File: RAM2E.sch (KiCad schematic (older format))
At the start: 63 parts, among them J1 AppleIIeAux, J2 JTAG, U1 EPM240T100, U2 W9864G6KH-6, U3 74AHC245, U4 74LVC245, U5 74AHC245, U6 74AHCT245, U7 74AHCT245, U8 TPS73701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

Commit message: As submitted to JLCPCB August 2020
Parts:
- removed C30: DNP, stdpads:C_0805, symbol Device:C_Small
- removed R1: 5k76, stdpads:R_0805, symbol Device:R_Small
- removed R2: 3k3, stdpads:R_0805, symbol Device:R_Small
- removed R3, R4, R8: DNP, stdpads:R_0805, symbol Device:R_Small
- removed R5: 0, stdpads:R_0805, symbol Device:R_Small
- removed U8: TPS73701, stdpads:SOT-223-6, symbol GW_Power:TPS73701
- removed U9: DNP, stdpads:SOT-223-6, symbol GW_Power:TPS73701
- added U8: AP2125N-3.3, stdpads:SOT-23, symbol GW_Power:AP2125
- C1, C2, C29, C3, C4, C5, C6: LCSC Part (none) -> C15850
- C10, C11, C12, C13, C14, C15, C16, C17, C18, C19, C20, C21, C22, C23, C24, C25, C26, C27, C28, C7, C8, C9: LCSC Part (none) -> C23630
- H1, H2, H3, H4: footprint stdpads:PasteHole_1.1mm_PTH -> stdpads:PasteHole_1.152mm_NPTH
- R10: LCSC Part (none) -> C17560
- R6: LCSC Part (none) -> C17477
- R9: value 1k2 -> 22k; LCSC Part (none) -> C17560
- RN1, RN2, RN3: value 4x100 -> 4x33; footprint stdpads:Yageo_YC124 -> stdpads:R4_0402; LCSC Part (none) -> C25501
- U1: LCSC Part (none) -> C10041
- U2: value W9864G6KH-6 -> W9812G6KH-6; LCSC Part (none) -> C62379
- U3, U5: LCSC Part (none) -> C5516
- U4: LCSC Part (none) -> C6082
- U6, U7: LCSC Part (none) -> C173388
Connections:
- net +1V8 is gone; now on net +3V3: C16.1, C19.1, C5.1, C6.1, U1.13 (VCCINT), U1.63 (VCCINT)
- net +3V3: now also C2.1, U8.2 (Vout)
- net +5V: now also U8.3 (Vin); no longer C2.1
- net ACLK: no longer RN3.6 (R3.2)
- net GND: now also U2.36 (A12), U8.1 (GND)
- net RCLK: no longer RN3.7 (R2.2)
- net at RN3.1 (R1.1), RN3.4 (R4.1), U4.18 (B0): no longer RN3.2 (R2.1), RN3.3 (R3.1)
- net CFG0: no longer names the net of U1.87 (IO2_87)
- net CFG1: no longer names the net of U1.86 (IO2_86)
- net CFG2: no longer names the net of U1.88 (IO2_88)
- net DlyIn: no longer names the net of U1.82 (IO2_82)
- net DlyOut: no longer names the net of U1.83 (IO2_83)
- no-connect marks 8 -> 17
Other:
- moved on the sheet: C1, C10, C11, C12, C13, C14, C15, C16, C17, C18, C19, C20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

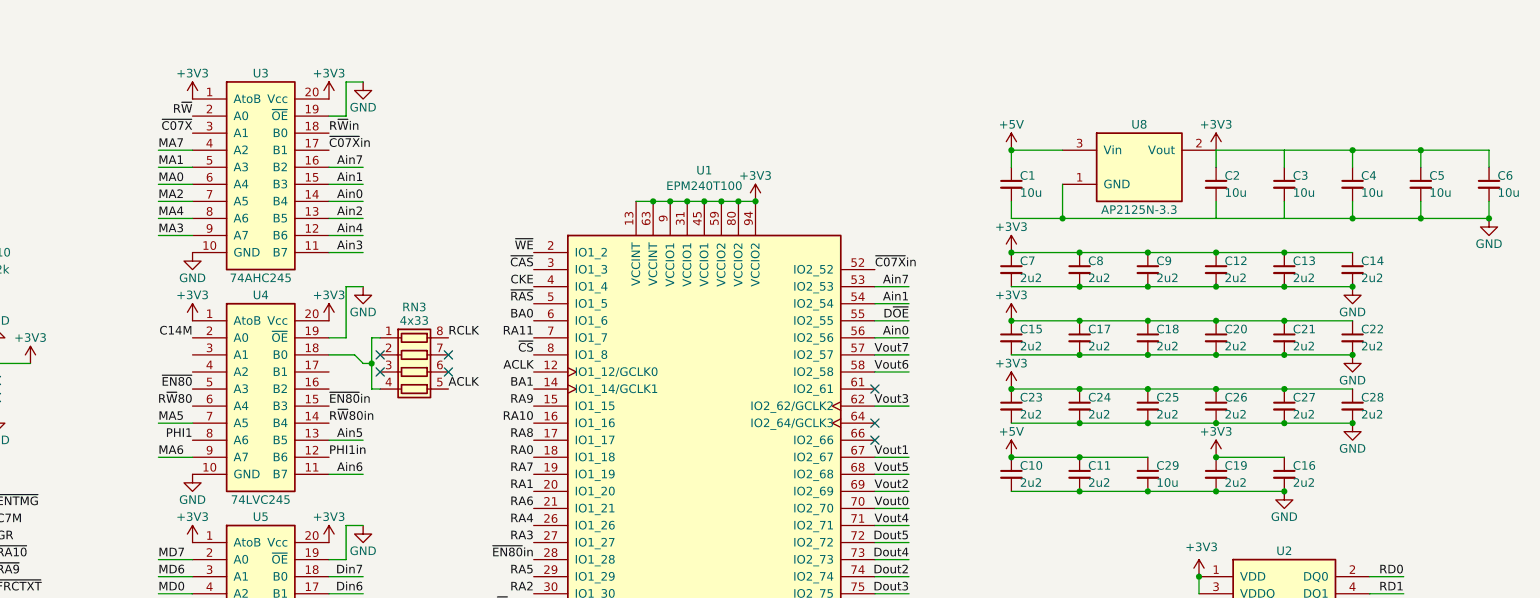
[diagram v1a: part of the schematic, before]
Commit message: Updated schematic with 1V8 regulator and MAX V
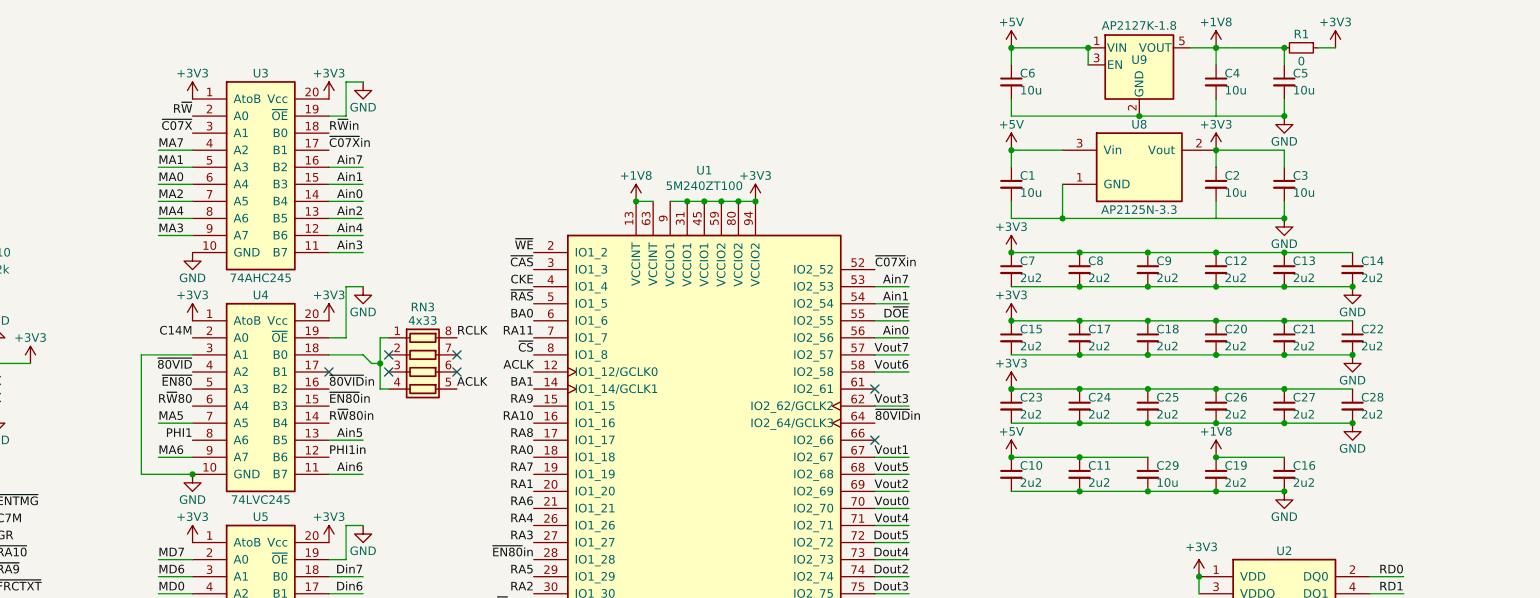
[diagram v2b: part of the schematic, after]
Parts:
- added R1: 0, stdpads:R_0805, symbol Device:R_Small
- added U9: AP2127K-1.8, stdpads:SOT-23-5, symbol Regulator_Linear:AP2127K-1.8
- U1: value EPM240T100 -> 5M240ZT100
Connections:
- net +3V3: now also R1.1; no longer C16.1, C19.1, C4.1, C5.1, C6.1, U1.13 (VCCINT), U1.63 (VCCINT)
- net +5V: now also C6.1, U9.1 (VIN), U9.3 (EN)
- net GND: now also U4.3 (A1), U9.2 (GND)
- net ~80VID~: now also U4.4 (A2)
- net ~80VID~in: now reaches U1.64 (IO2_64/GCLK3)
- net ~80VID~in: now also U4.16 (B2)
- new net +1V8: C16.1, C19.1, C4.1, C5.1, R1.2, U1.13 (VCCINT), U1.63 (VCCINT), U9.5 (VOUT)
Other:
- moved on the sheet: C4, C5, RN3

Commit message: Merge branch 'dev-GW4203B-1.2' of https://github.com/garrettsworkshop/RAM2E into dev-GW4203B-1.2
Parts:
- added RN4, RN5: 4x33, stdpads:R4_0402, symbol Device:R_Pack04
- R1: value 0 -> DNP
- U1: LCSC Part C10041 -> C192889
- U3, U5: value 74AHC245 -> 74LVC245; LCSC Part C5516 -> C6082
- U8: value AP2125N-3.3 -> XC6206P332MR; LCSC Part C150715 -> C5446
- U9: LCSC Part (none) -> C151375
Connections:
- net Ain0: now also RN5.8 (R1.2); no longer U3.14 (B4)
- net Ain1: now also RN4.5 (R4.2); no longer U3.15 (B3)
- net Ain2: now also RN5.7 (R2.2); no longer U3.13 (B5)
- net Ain3: now also RN5.5 (R4.2); no longer U3.11 (B7)
- net Ain4: now also RN5.6 (R3.2); no longer U3.12 (B6)
- net Ain7: now also RN4.6 (R3.2); no longer U3.16 (B2)
- net GND: now also U4.4 (A2)
- net R~W~in: now also RN4.8 (R1.2); no longer U3.18 (B0)
- net ~80VID~: no longer U4.4 (A2)
- net ~80VID~in: no longer U4.16 (B2)
- net ~C07X~in: now also RN4.7 (R2.2); no longer U3.17 (B1)
- new net: RN5.4 (R4.1), U3.11 (B7)
- new net: RN5.3 (R3.1), U3.12 (B6)
- new net: RN5.2 (R2.1), U3.13 (B5)
- new net: RN5.1 (R1.1), U3.14 (B4)
- new net: RN4.4 (R4.1), U3.15 (B3)
- new net: RN4.3 (R3.1), U3.16 (B2)
- new net: RN4.2 (R2.1), U3.17 (B1)
- new net: RN4.1 (R1.1), U3.18 (B0)
- no-connect marks 17 -> 18
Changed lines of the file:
@@
 Sheet 1 2
 Title "GW4203B (RAM2E II)"
-Date "2020-08-04"
-Rev "1.1"
+Date "2020-09-10"
+Rev "1.2"
 Comp "Garrett's Workshop"
 Comment1 ""
@@
 P 3000 1500
 F 0 "U3" H 3000 2100 50  0000 C CNN
-F 1 "74AHC245" H 3000 900 50  0000 C CNN
+F 1 "74LVC245" H 3000 900 50  0000 C CNN
 F 2 "stdpads:TSSOP-20_4.4x6.5mm_P0.65mm" H 3000 850 50  0001 C TNN
 F 3 "" H 3000 1600 60  0001 C CNN
-F 4 "C5516" H 3000 1500 50  0001 C CNN "LCSC Part"
+F 4 "C6082" H 3000 1500 50  0001 C CNN "LCSC Part"
 	1    3000 1500
 	1    0    0    -1
@@
 L power:GND #PWR0104
 U 1 1 5E9BEAE2
-P 3600 950
-F 0 "#PWR0104" H 3600 700 50  0001 C CNN
-F 1 "GND" H 3600 800 50  0000 C CNN
-F 2 "" H 3600 950 50  0001 C CNN
-F 3 "" H 3600 950 50  0001 C CNN
-	1    3600 950
-	1    0    0    -1
-$EndComp
-Wire Wire Line
-	3500 1150 3500 950
-Wire Wire Line
-	3500 950  3600 950
+P 3600 850
+F 0 "#PWR0104" H 3600 600 50  0001 C CNN
+F 1 "GND" H 3600 700 50  0000 C CNN
+F 2 "" H 3600 850 50  0001 C CNN
+F 3 "" H 3600 850 50  0001 C CNN
+	1    3600 850
+	1    0    0    -1
+$EndComp
+Wire Wire Line
+	3500 850  3600 850
 Wire Wire Line
 	3400 1150 3500 1150
@@
 Wire Wire Line
 	8500 5150 8300 5150
-Text Label 3400 1350 0    50   ~ 0
+Text Label 3800 1350 0    50   ~ 0
 ~C07X~in
 Text Label 3400 2950 0    50   ~ 0
@@
 Text Label 3400 2850 0    50   ~ 0
 ~EN80~in
-Text Label 3400 1250 0    50   ~ 0
+Text Label 3800 1250 0    50   ~ 0
 R~W~in
 Text Label 3400 3150 0    50   ~ 0
@@
 P 3000 4100
 F 0 "U5" H 3000 4700 50  0000 C CNN
-F 1 "74AHC245" H 3000 3500 50  0000 C CNN
+F 1 "74LVC245" H 3000 3500 50  0000 C CNN
 F 2 "stdpads:TSSOP-20_4.4x6.5mm_P0.65mm" H 3000 3450 50  0001 C TNN
 F 3 "" H 3000 4200 60  0001 C CNN
-F 4 "C5516" H 3000 4100 50  0001 C CNN "LCSC Part"
+F 4 "C6082" H 3000 4100 50  0001 C CNN "LCSC Part"
 	1    3000 4100
 	1    0    0    -1
@@
 L power:GND #PWR0126
 U 1 1 5F3A4A01
-P 3600 2150
-F 0 "#PWR0126" H 3600 1900 50  0001 C CNN
-F 1 "GND" H 3600 2000 50  0000 C CNN
-F 2 "" H 3600 2150 50  0001 C CNN
-F 3 "" H 3600 2150 50  0001 C CNN
-	1    3600 2150
-	1    0    0    -1
-$EndComp
-Wire Wire Line
-	3500 2150 3600 2150
+P 3600 2350
+F 0 "#PWR0126" H 3600 2100 50  0001 C CNN
+F 1 "GND" H 3600 2200 50  0000 C CNN
+F 2 "" H 3600 2350 50  0001 C CNN
+F 3 "" H 3600 2350 50  0001 C CNN
+	1    3600 2350
+	1    0    0    -1
+$EndComp
+Wire Wire Line
+	3500 2350 3600 2350
 Wire Wire Line
 	3400 2450 3500 2450
@@
 R~W~80
 Wire Wire Line
-	3600 1750 3400 1750
-Wire Wire Line
-	3600 1950 3400 1950
-Wire Wire Line
-	3600 1850 3400 1850
+	4000 1750 3800 1750
+Wire Wire Line
+	4000 1950 3800 1950
+Wire Wire Line
+	4000 1850 3800 1850
 Wire Wire Line
 	3600 3050 3400 3050
 Wire Wire Line
-	3600 1450 3400 1450
-Text Label 3600 1750 2    50   ~ 0
+	4000 1450 3800 1450
+Text Label 4000 1750 2    50   ~ 0
 Ain2
-Text Label 3600 1950 2    50   ~ 0
+Text Label 4000 1950 2    50   ~ 0
 Ain3
 Text Label 3600 3250 2    50   ~ 0
 Ain6
-Text Label 3600 1850 2    50   ~ 0
+Text Label 4000 1850 2    50   ~ 0
 Ain4
 Text Label 3600 3050 2    50   ~ 0
 Ain5
-Text Label 3600 1450 2    50   ~ 0
+Text Label 4000 1450 2    50   ~ 0
 Ain7
 Wire Wire Line
-	3600 1550 3400 1550
-Text Label 3600 1650 2    50   ~ 0
+	4000 1550 3800 1550
+Text Label 4000 1650 2    50   ~ 0
 Ain0
-Text Label 3600 1550 2    50   ~ 0
+Text Label 4000 1550 2    50   ~ 0
 Ain1
 Wire Wire Line
-	3600 1650 3400 1650
+	4000 1650 3800 1650
 Text Label 2600 1150 2    50   ~ 0
 R~W~
@@
 Wire Wire Line
 	5200 1650 5300 1650
-Wire Wire Line
-	3500 2150 3500 2450
 Text Label 4150 2750 0    50   ~ 0
 ACLK
@@
 F 2 "stdpads:TQFP-100_14x14mm_P0.5mm" H 6000 1700 50  0001 L CNN
 F 3 "https://www.altera.com/content/dam/altera-www/global/en_US/pdfs/literature/hb/max2/max2_mii5v1.pdf" H 5600 4050 50  0001 C CNN
-F 4 "C10041" H 5600 4050 50  0001 C CNN "LCSC Part"
+F 4 "C192889" H 5600 4050 50  0001 C CNN "LCSC Part"
 	1    5600 4050
 	1    0    0    -1
@@
 P 8150 1450
 F 0 "U8" H 8150 1700 50  0000 C CNN
-F 1 "AP2125N-3.3" H 8150 1200 50  0000 C CNN
+F 1 "XC6206P332MR" H 8150 1200 50  0000 C CNN
 F 2 "stdpads:SOT-23" H 8150 1150 50  0001 C TNN
 F 3 "" H 8150 1350 60  0001 C CNN
-F 4 "C150715" H 8150 1450 50  0001 C CNN "LCSC Part"
+F 4 "C5446" H 8150 1450 50  0001 C CNN "LCSC Part"
 	1    8150 1450
 	1    0    0    -1
@@
 Wire Wire Line
 	8600 1750 8600 1650
-Text Label 2600 2650 2    50   ~ 0
-~80VID~
-Text Label 3400 2750 0    50   ~ 0
-~80VID~in
 Wire Wire Line
 	3600 2550 3650 2600
@@
 	3400 2550 3600 2550
 NoConn ~ 3400 2650
-Wire Wire Line
-	2600 2550 2300 2550
 Wire Wire Line
 	2300 2550 2300 3250
@@
 F 2 "stdpads:SOT-23-5" H 8150 1175 50  0001 C CNN
 F 3 "https://www.diodes.com/assets/Datasheets/AP2127.pdf" H 8150 950 50  0001 C CNN
+F 4 "C151375" H 8150 850 50  0001 C CNN "LCSC Part"
 	1    8150 850
 	1    0    0    -1
@@
 P 9100 750
 F 0 "R1" V 9050 750 50  0000 C BNN
-F 1 "0" V 9150 750 50  0000 C TNN
+F 1 "DNP" V 9150 750 50  0000 C TNN
 F 2 "stdpads:R_0805" H 9100 750 50  0001 C CNN
 F 3 "~" H 9100 750 50  0001 C CNN
@@
 Wire Wire Line
 	9300 750  9200 750
+Wire Wire Line
+	2600 2550 2300 2550
+Wire Wire Line
+	2600 2550 2600 2650
+Connection ~ 2600 2550
+NoConn ~ 3400 2750
+$Comp
+L Device:R_Pack04 RN5
+U 1 1 5F6F2814
+P 3600 1850
+F 0 "RN5" V 3900 1850 50  0000 C BNN
+F 1 "4x33" V 3800 1850 50  0000 C CNN
+F 2 "stdpads:R4_0402" V 3875 1850 50  0001 C CNN
+F 3 "~" H 3600 1850 50  0001 C CNN
+F 4 "C25501" H 3600 1850 50  0001 C CNN "LCSC Part"
+	1    3600 1850
+	0    1    1    0
+$EndComp
+$Comp
+L Device:R_Pack04 RN4
+U 1 1 5F68B09A
+P 3600 1450
+F 0 "RN4" V 3250 1450 50  0000 C BNN
+F 1 "4x33" V 3300 1450 50  0000 C CNN
+F 2 "stdpads:R4_0402" V 3875 1450 50  0001 C CNN
+F 3 "~" H 3600 1450 50  0001 C CNN
+F 4 "C25501" H 3600 1450 50  0001 C CNN "LCSC Part"
+	1    3600 1450
+	0    1    1    0
+$EndComp
+Wire Wire Line
+	3500 850  3500 1150
+Wire Wire Line
+	3500 2350 3500 2450
 Wire Bus Line
 	8200 4250 8200 5350

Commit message: Actually fabbed 10/6/2020
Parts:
- U1: value 5M240ZT100 -> 5M240ZT100C5N
- U3, U4, U5: value 74LVC245 -> 74LVC245APW
- U6, U7: value 74AHCT245 -> 74AHCT245PW
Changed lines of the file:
@@
 Sheet 1 2
 Title "GW4203B (RAM2E II)"
-Date "2020-09-10"
+Date "2020-09-29"
 Rev "1.2"
 Comp "Garrett's Workshop"
@@
 P 3000 1500
 F 0 "U3" H 3000 2100 50  0000 C CNN
-F 1 "74LVC245" H 3000 900 50  0000 C CNN
+F 1 "74LVC245APW" H 3000 900 50  0000 C CNN
 F 2 "stdpads:TSSOP-20_4.4x6.5mm_P0.65mm" H 3000 850 50  0001 C TNN
 F 3 "" H 3000 1600 60  0001 C CNN
@@
 P 3000 5400
 F 0 "U6" H 3000 6000 50  0000 C CNN
-F 1 "74AHCT245" H 3000 4800 50  0000 C CNN
+F 1 "74AHCT245PW" H 3000 4800 50  0000 C CNN
 F 2 "stdpads:TSSOP-20_4.4x6.5mm_P0.65mm" H 3000 4750 50  0001 C TNN
 F 3 "" H 3000 5500 60  0001 C CNN
@@
 P 3000 4100
 F 0 "U5" H 3000 4700 50  0000 C CNN
-F 1 "74LVC245" H 3000 3500 50  0000 C CNN
+F 1 "74LVC245APW" H 3000 3500 50  0000 C CNN
 F 2 "stdpads:TSSOP-20_4.4x6.5mm_P0.65mm" H 3000 3450 50  0001 C TNN
 F 3 "" H 3000 4200 60  0001 C CNN
@@
 P 3000 6700
 F 0 "U7" H 3000 7300 50  0000 C CNN
-F 1 "74AHCT245" H 3000 6100 50  0000 C CNN
+F 1 "74AHCT245PW" H 3000 6100 50  0000 C CNN
 F 2 "stdpads:TSSOP-20_4.4x6.5mm_P0.65mm" H 3000 6050 50  0001 C TNN
 F 3 "" H 3000 6800 60  0001 C CNN
@@
 P 3000 2800
 F 0 "U4" H 3000 3400 50  0000 C CNN
-F 1 "74LVC245" H 3000 2200 50  0000 C CNN
+F 1 "74LVC245APW" H 3000 2200 50  0000 C CNN
 F 2 "stdpads:TSSOP-20_4.4x6.5mm_P0.65mm" H 3000 2150 50  0001 C TNN
 F 3 "" H 3000 2900 60  0001 C CNN
@@
 U 1 1 5EF407E5
 P 5600 4050
-F 0 "U1" H 5600 6631 50  0000 C CNN
-F 1 "5M240ZT100" H 5600 6540 50  0000 C CNN
+F 0 "U1" H 5550 6550 50  0000 C BNN
+F 1 "5M240ZT100C5N" H 5550 6500 50  0000 C CNN
 F 2 "stdpads:TQFP-100_14x14mm_P0.5mm" H 6000 1700 50  0001 L CNN
 F 3 "https://www.altera.com/content/dam/altera-www/global/en_US/pdfs/literature/hb/max2/max2_mii5v1.pdf" H 5600 4050 50  0001 C CNN

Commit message: Added C14M buffering and header
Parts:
- added J3: C14M, Connector_PinHeader_2.54mm:PinHeader_1x02_P2.54mm_Vertical, symbol Connector_Generic:Conn_01x02
- added R2, R3: 33, stdpads:R_0603, symbol Device:R_Small
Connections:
- net C14M: now also R2.2; no longer U4.2 (A0)
- net GND: now also J3.2 (Pin_2); no longer U4.4 (A2)
- net at U4.16 (B2): now also R3.2
- new net C14MB: J3.1 (Pin_1), R3.1
- new net C14MR: R2.1, U4.2 (A0), U4.4 (A2)
- no-connect marks 18 -> 17
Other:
- moved on the sheet: RN3
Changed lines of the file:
@@
 Text Label 2400 1450 0    50   ~ 0
 MA1
-Text Label 2600 2450 2    50   ~ 0
+Text Label 2150 2450 2    50   ~ 0
 C14M
 $Comp
@@
 Text Label 4600 2650 2    50   ~ 0
 ACLK
-Text Label 4150 2450 0    50   ~ 0
+Text Label 4150 2300 0    50   ~ 0
 RCLK
 Text Label 4600 2850 2    50   ~ 0
@@
 Wire Wire Line
 	5200 1650 5300 1650
-Text Label 4150 2750 0    50   ~ 0
+Text Label 4150 2600 0    50   ~ 0
 ACLK
 $Comp
 L Device:R_Pack04 RN3
 U 1 1 5F475CD8
-P 3950 2650
-F 0 "RN3" V 3600 2650 50  0000 C BNN
-F 1 "4x33" V 3650 2650 50  0000 C CNN
-F 2 "stdpads:R4_0402" V 4225 2650 50  0001 C CNN
-F 3 "~" H 3950 2650 50  0001 C CNN
-F 4 "C25501" H 3950 2650 50  0001 C CNN "LCSC Part"
-	1    3950 2650
+P 3950 2500
+F 0 "RN3" V 3600 2500 50  0000 C BNN
+F 1 "4x33" V 3650 2500 50  0000 C CNN
+F 2 "stdpads:R4_0402" V 4225 2500 50  0001 C CNN
+F 3 "~" H 3950 2500 50  0001 C CNN
+F 4 "C25501" H 3950 2500 50  0001 C CNN "LCSC Part"
+	1    3950 2500
 	0    1    1    0
 $EndComp
@@
 NoConn ~ 6600 5050
 Wire Wire Line
-	3750 2450 3700 2450
-Wire Wire Line
-	3700 2750 3750 2750
-NoConn ~ 4150 2550
-NoConn ~ 4150 2650
-NoConn ~ 3750 2550
-NoConn ~ 3750 2650
-Wire Wire Line
-	3700 2450 3700 2600
+	3750 2300 3700 2300
+Wire Wire Line
+	3700 2600 3750 2600
+NoConn ~ 4150 2400
+NoConn ~ 4150 2500
+NoConn ~ 3750 2400
+NoConn ~ 3750 2500
 Wire Wire Line
 	3650 2600 3700 2600
 Connection ~ 3700 2600
-Wire Wire Line
-	3700 2600 3700 2750
 $Comp
 L power:GND #PWR0146
@@
 NoConn ~ 3400 2650
 Wire Wire Line
-	2300 2550 2300 3250
-Wire Wire Line
 	2300 3250 2600 3250
 Connection ~ 2600 3250
@@
 Wire Wire Line
 	9300 750  9200 750
-Wire Wire Line
-	2600 2550 2300 2550
-Wire Wire Line
-	2600 2550 2600 2650
-Connection ~ 2600 2550
-NoConn ~ 3400 2750
 $Comp
 L Device:R_Pack04 RN5
@@
 Wire Wire Line
 	3500 2350 3500 2450
+Wire Wire Line
+	2600 2550 2300 2550
+Wire Wire Line
+	2300 2550 2300 3250
+Wire Wire Line
+	2500 2450 2500 2650
+Wire Wire Line
+	2500 2650 2600 2650
+Wire Wire Line
+	2600 2450 2500 2450
+Wire Wire Line
+	3700 2300 3700 2600
+$Comp
+L Device:R_Small R3
+U 1 1 6081D682
+P 3950 2750
+F 0 "R3" V 4000 2750 50  0000 C TNN
+F 1 "33" V 4100 2750 50  0000 C CNN
+F 2 "stdpads:R_0603" H 3950 2750 50  0001 C CNN
+F 3 "~" H 3950 2750 50  0001 C CNN
+	1    3950 2750
+	0    1    1    0
+$EndComp
+Wire Wire Line
+	3400 2750 3850 2750
+$Comp
+L Connector_Generic:Conn_01x02 J3
+U 1 1 608879CA
+P 1050 1150
+F 0 "J3" H 1050 1250 50  0000 C CNN
+F 1 "C14M" H 1050 950 50  0000 C CNN
+F 2 "Connector_PinHeader_2.54mm:PinHeader_1x02_P2.54mm_Vertical" H 1050 1150 50  0001 C CNN
+F 3 "~" H 1050 1150 50  0001 C CNN
+	1    1050 1150
+	-1   0    0    -1
+$EndComp
+Text Label 1250 1150 0    50   ~ 0
+C14MB
+$Comp
+L power:GND #PWR0147
+U 1 1 6088870C
+P 1250 1250
+F 0 "#PWR0147" H 1250 1000 50  0001 C CNN
+F 1 "GND" H 1250 1100 50  0000 C CNN
+F 2 "" H 1250 1250 50  0001 C CNN
+F 3 "" H 1250 1250 50  0001 C CNN
+	1    1250 1250
+	1    0    0    -1
+$EndComp
+Text Label 4050 2750 0    50   ~ 0
+C14MB
+$Comp
+L Device:R_Small R2
+U 1 1 6088A353
+P 2250 2450
+F 0 "R2" V 2400 2450 50  0000 C CNN
+F 1 "33" V 2300 2450 50  0000 C TNN
+F 2 "stdpads:R_0603" H 2250 2450 50  0001 C CNN
+F 3 "~" H 2250 2450 50  0001 C CNN
+	1    2250 2450
+	0    1    -1   0
+$EndComp
+Text Label 2600 2450 2    50   ~ 0
+C14MR
+Wire Wire Line
+	2350 2450 2500 2450
 Wire Bus Line
 	8200 4250 8200 5350
+Connection ~ 2500 2450
 $EndSCHEMATC

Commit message: Fabbed
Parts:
- R1: value DNP -> 0; LCSC Part (none) -> C17477
- R2, R3: value 33 -> 47; LCSC Part (none) -> C23182
- U1: value 5M240ZT100C5N -> EPM240T100C5N; LCSC Part C192889 -> C10041
- U9: value AP2127K-1.8 -> DNP; LCSC Part C151375 -> (none)
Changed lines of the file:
@@
 Sheet 1 2
 Title "GW4203B (RAM2E II)"
-Date "2020-09-29"
-Rev "1.2"
+Date "2020-12-25"
+Rev "1.3"
 Comp "Garrett's Workshop"
 Comment1 ""
@@
 P 5600 4050
 F 0 "U1" H 5550 6550 50  0000 C BNN
-F 1 "5M240ZT100C5N" H 5550 6500 50  0000 C CNN
+F 1 "EPM240T100C5N" H 5550 6500 50  0000 C CNN
 F 2 "stdpads:TQFP-100_14x14mm_P0.5mm" H 6000 1700 50  0001 L CNN
 F 3 "https://www.altera.com/content/dam/altera-www/global/en_US/pdfs/literature/hb/max2/max2_mii5v1.pdf" H 5600 4050 50  0001 C CNN
-F 4 "C192889" H 5600 4050 50  0001 C CNN "LCSC Part"
+F 4 "C10041" H 5600 4050 50  0001 C CNN "LCSC Part"
 	1    5600 4050
 	1    0    0    -1
@@
 	3400 2550 3600 2550
 NoConn ~ 3400 2650
-Wire Wire Line
-	2300 3250 2600 3250
 Connection ~ 2600 3250
 Text Label 6600 2950 0    50   ~ 0
@@
 P 8150 850
 F 0 "U9" H 8150 850 50  0000 C BNN
-F 1 "AP2127K-1.8" H 8150 1050 50  0000 C BNN
+F 1 "DNP" H 8150 1050 50  0000 C BNN
 F 2 "stdpads:SOT-23-5" H 8150 1175 50  0001 C CNN
 F 3 "https://www.diodes.com/assets/Datasheets/AP2127.pdf" H 8150 950 50  0001 C CNN
-F 4 "C151375" H 8150 850 50  0001 C CNN "LCSC Part"
+F 4 "" H 8150 850 50  0001 C CNN "LCSC Part"
 	1    8150 850
 	1    0    0    -1
@@
 P 9100 750
 F 0 "R1" V 9050 750 50  0000 C BNN
-F 1 "DNP" V 9150 750 50  0000 C TNN
+F 1 "0" V 9150 750 50  0000 C TNN
 F 2 "stdpads:R_0805" H 9100 750 50  0001 C CNN
 F 3 "~" H 9100 750 50  0001 C CNN
+F 4 "C17477" V 9100 750 50  0001 C CNN "LCSC Part"
 	1    9100 750
 	0    1    1    0
@@
 	3500 2350 3500 2450
 Wire Wire Line
-	2600 2550 2300 2550
-Wire Wire Line
-	2300 2550 2300 3250
-Wire Wire Line
-	2500 2450 2500 2650
-Wire Wire Line
-	2500 2650 2600 2650
-Wire Wire Line
-	2600 2450 2500 2450
-Wire Wire Line
 	3700 2300 3700 2600
 $Comp
@@
 P 3950 2750
 F 0 "R3" V 4000 2750 50  0000 C TNN
-F 1 "33" V 4100 2750 50  0000 C CNN
+F 1 "47" V 4100 2750 50  0000 C CNN
 F 2 "stdpads:R_0603" H 3950 2750 50  0001 C CNN
 F 3 "~" H 3950 2750 50  0001 C CNN
+F 4 "C23182" V 3950 2750 50  0001 C CNN "LCSC Part"
 	1    3950 2750
 	0    1    1    0
@@
 P 2250 2450
 F 0 "R2" V 2400 2450 50  0000 C CNN
-F 1 "33" V 2300 2450 50  0000 C TNN
+F 1 "47" V 2300 2450 50  0000 C TNN
 F 2 "stdpads:R_0603" H 2250 2450 50  0001 C CNN
 F 3 "~" H 2250 2450 50  0001 C CNN
+F 4 "C23182" V 2250 2450 50  0001 C CNN "LCSC Part"
 	1    2250 2450
 	0    1    -1   0
@@
 C14MR
 Wire Wire Line
+	2300 3250 2600 3250
+Wire Wire Line
+	2600 2550 2300 2550
+Wire Wire Line
+	2300 2550 2300 3250
+Wire Wire Line
+	2500 2650 2600 2650
+Connection ~ 2500 2450
+Wire Wire Line
 	2350 2450 2500 2450
+Wire Wire Line
+	2600 2450 2500 2450
+Wire Wire Line
+	2500 2450 2500 2650
 Wire Bus Line
 	8200 4250 8200 5350
-Connection ~ 2500 2450
 $EndSCHEMATC
